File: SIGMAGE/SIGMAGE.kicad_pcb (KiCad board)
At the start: 6 copper layers, 100 x 85 mm, 128 parts, among them J1 UJ31CHG2SMTTR, J10 TSW10607GS, J11 HTSW10807GD, J12 HTSW10807GD, J13 HTSW10807GD, J14 HTSW10807GD, J15 HTSW10807GD, J16 HTSW10807GD, J17 HTSW10807GD, J18 HTSW10107GD, J19 HTSW10107GD, J2 SJ63073E, J20 HTSW10107GD, J3 SJ63073E, J4 SJ63073E, J5 SJ63073E, J6 ARJM11D7502ABEW2, J7 TSW10607GS, J8 TSW10607GS, J9 TSW10607GS, U1 MAX8902BATA/V+T, U2 MAX8902BATA/V+T, U3 MAX8902BATA/V+T, U4 OPA1612AIDRGR, U5 PCM1803ADB, U6 OPA1612AIDRGR, U7 PCM1803ADB, U8 STM32F407VGTx, U9 LAN8720ACP, X1 STDCSU18M, X2 STDCSK425M

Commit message: Makin it waaay cheaper and JLCPCB conform
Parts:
- removed C58: 1u, Capacitor_SMD:C_0603_1608Metric
- removed C7, C9: 10u, Capacitor_SMD:C_0603_1608Metric
- removed C8: 10n, Capacitor_SMD:C_0603_1608Metric
- removed FB3: 500 @ 100 MHz, Capacitor_SMD:C_0603_1608Metric
- removed J20: HTSW10107GD, SIGMAGE:HTSW10107GD
- removed R7, R8: 120k, Resistor_SMD:R_0603_1608Metric
- removed U3: MAX8902BATA/V+T, SIGMAGE:MAX8902BATAVT
- C28, C29, C30, C31, C32, C33, C34, C35, C40, C53: moved to B.Cu
- moved J11 324.9 mm to (375.4, 28.8)
- moved J12 324.9 mm to (375.4, 36.4)
- moved J13 324.9 mm to (375.4, 44.1)
- moved C14 139.7 mm to (180.2, 100.8)
- moved C15 138.6 mm to (166.5, 99.5)
- moved C34 106.6 mm to (144.2, 131.0), turned to 180 degrees
- moved C35 104.5 mm to (144.2, 129.5), turned to 180 degrees
- moved C49 102.0 mm to (111.2, 121.8), turned to -90 degrees
- moved C50 98.8 mm to (112.8, 121.8), turned to -90 degrees
- moved J19 98.7 mm to (180.5, 142.5)
- moved D2 98.3 mm to (176.0, 145.5), turned to 90 degrees
- moved C51 98.1 mm to (106.5, 117.5), turned to 90 degrees
- moved C52 98.1 mm to (106.5, 120.5), turned to -90 degrees
- moved D4 97.6 mm to (194.0, 137.2), turned to -90 degrees
- moved R5 96.5 mm to (173.0, 146.0), turned to 180 degrees
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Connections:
- J11 pad 1: GPIO_PE14 -> unconnected-(J11-Pad1)
- J11 pad 10: GPIO_PE7 -> unconnected-(J11-Pad10)
- J11 pad 11: GPIO_PB2 -> unconnected-(J11-Pad11)
- J11 pad 12: GPIO_PB1 -> unconnected-(J11-Pad12)
- J11 pad 13: GPIO_PB0 -> unconnected-(J11-Pad13)
- J11 pad 14: GPIO_PA6 -> unconnected-(J11-Pad14)
- J11 pad 15: GPIO_PA5 -> unconnected-(J11-Pad15)
- J11 pad 16: GPIO_PA3 -> unconnected-(J11-Pad16)
- J11 pad 2: GPIO_PE12 -> unconnected-(J11-Pad2)
- J11 pad 3: GPIO_PE15 -> unconnected-(J11-Pad3)
- J11 pad 4: GPIO_PE13 -> unconnected-(J11-Pad4)
- J11 pad 5: GPIO_PB14 -> unconnected-(J11-Pad5)
- J11 pad 6: GPIO_PE11 -> unconnected-(J11-Pad6)
- J11 pad 7: GPIO_PE10 -> unconnected-(J11-Pad7)
- J11 pad 8: GPIO_PE9 -> unconnected-(J11-Pad8)
- J11 pad 9: GPIO_PE8 -> unconnected-(J11-Pad9)
- J12 pad 1: GPIO_PC3 -> unconnected-(J12-Pad1)
- J12 pad 10: GPIO_PD5 -> unconnected-(J12-Pad10)
- J12 pad 11: GPIO_PE0 -> unconnected-(J12-Pad11)
- J12 pad 12: GPIO_PD7 -> unconnected-(J12-Pad12)
- J12 pad 13: GPIO_PE4 -> unconnected-(J12-Pad13)
- J12 pad 14: GPIO_PE1 -> unconnected-(J12-Pad14)
- J12 pad 15: GPIO_PE2 -> unconnected-(J12-Pad15)
- J12 pad 16: GPIO_PE3 -> unconnected-(J12-Pad16)
- J12 pad 2: GPIO_PA0 -> unconnected-(J12-Pad2)
- J12 pad 3: GPIO_PC0 -> unconnected-(J12-Pad3)
- J12 pad 4: GPIO_PC2 -> unconnected-(J12-Pad4)
- J12 pad 5: GPIO_PC14 -> unconnected-(J12-Pad5)
- J12 pad 6: GPIO_PC15 -> unconnected-(J12-Pad6)
- J12 pad 7: GPIO_PE5 -> unconnected-(J12-Pad7)
- J12 pad 8: GPIO_PE6 -> unconnected-(J12-Pad8)
- J12 pad 9: GPIO_PD6 -> unconnected-(J12-Pad9)
- J13 pad 1: GPIO_PC11 -> unconnected-(J13-Pad1)
- J13 pad 10: GPIO_PD10 -> unconnected-(J13-Pad10)
- J13 pad 11: GPIO_PD4 -> unconnected-(J13-Pad11)
- J13 pad 12: GPIO_PD8 -> unconnected-(J13-Pad12)
- J13 pad 13: GPIO_PD0 -> unconnected-(J13-Pad13)
- J13 pad 14: GPIO_PD3 -> unconnected-(J13-Pad14)
- J13 pad 15: GPIO_PD1 -> unconnected-(J13-Pad15)
- J13 pad 16: GPIO_PD2 -> unconnected-(J13-Pad16)
- J13 pad 2: GPIO_PC8 -> unconnected-(J13-Pad2)
- J13 pad 3: GPIO_PC9 -> unconnected-(J13-Pad3)
- J13 pad 4: GPIO_PD15 -> unconnected-(J13-Pad4)
- J13 pad 5: GPIO_PD13 -> unconnected-(J13-Pad5)
- J13 pad 6: GPIO_PD14 -> unconnected-(J13-Pad6)
- J13 pad 7: GPIO_PD11 -> unconnected-(J13-Pad7)
- J13 pad 8: GPIO_PD12 -> unconnected-(J13-Pad8)
- J13 pad 9: GPIO_PD9 -> unconnected-(J13-Pad9)
- J14 pad 1: +3V3 -> +5V
- J14 pad 10: +3V3 -> +5V
- J14 pad 11: +3V3 -> +5V
- J14 pad 12: +3V3 -> +5V
- J14 pad 13: +3V3 -> +5V
- J14 pad 14: +3V3 -> +5V
- J14 pad 15: +3V3 -> +5V
- J14 pad 16: +3V3 -> +5V
- J14 pad 2: +3V3 -> +5V
- J14 pad 3: +3V3 -> +5V
- J14 pad 4: +3V3 -> +5V
- J14 pad 5: +3V3 -> +5V
- J14 pad 6: +3V3 -> +5V
- J14 pad 7: +3V3 -> +5V
- J14 pad 8: +3V3 -> +5V
- J14 pad 9: +3V3 -> +5V
- J15 pad 1: +2V5 -> +3V3
- J15 pad 10: +2V5 -> +3V3
- J15 pad 11: +2V5 -> +3V3
- J15 pad 12: +2V5 -> +3V3
- J15 pad 13: +2V5 -> +3V3
- J15 pad 14: +2V5 -> +3V3
- J15 pad 15: +2V5 -> +3V3
- J15 pad 16: +2V5 -> +3V3
- J15 pad 2: +2V5 -> +3V3
- J15 pad 3: +2V5 -> +3V3
- J15 pad 4: +2V5 -> +3V3
- J15 pad 5: +2V5 -> +3V3
- J15 pad 6: +2V5 -> +3V3
- J15 pad 7: +2V5 -> +3V3
- J15 pad 8: +2V5 -> +3V3
- J15 pad 9: +2V5 -> +3V3
- J16 pad 1: +1V2 -> +2V5
- J16 pad 10: +1V2 -> +2V5
- J16 pad 11: +1V2 -> +2V5
- J16 pad 12: +1V2 -> +2V5
- J16 pad 13: +1V2 -> +2V5
- J16 pad 14: +1V2 -> +2V5
- J16 pad 15: +1V2 -> +2V5
- J16 pad 16: +1V2 -> +2V5
- J16 pad 2: +1V2 -> +2V5
- J16 pad 3: +1V2 -> +2V5
- J16 pad 4: +1V2 -> +2V5
- J16 pad 5: +1V2 -> +2V5
- J16 pad 6: +1V2 -> +2V5
- J16 pad 7: +1V2 -> +2V5
- J16 pad 8: +1V2 -> +2V5
- J16 pad 9: +1V2 -> +2V5
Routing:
- net GND: track 157.6 -> 0.00 mm, vias 47 -> 0
- net +5V: track 122.0 -> 0.00 mm, vias 12 -> 0
- net GPIO_PD0: track 78.9 -> 0.00 mm, vias 1 -> 0
- net GPIO_PD4: track 73.5 -> 0.00 mm, vias 1 -> 0
- net GPIO_PD1: track 72.1 -> 0.00 mm, vias 1 -> 0
- net GPIO_PD3: track 70.3 -> 0.00 mm, vias 1 -> 0
- net GPIO_PD2: track 67.8 -> 0.00 mm, vias 1 -> 0
- net +3V3: track 70.1 -> 10.6 mm, vias 17 -> 0
- net GPIO_PC11: track 56.6 -> 0.00 mm, vias 1 -> 0
- net GPIO_PD6: track 52.4 -> 0.00 mm, vias 1 -> 0
- net GPIO_PD13: track 51.8 -> 0.00 mm, vias 1 -> 0
- net GPIO_PD11: track 51.8 -> 0.00 mm, vias 1 -> 0
- net GPIO_PE0: track 51.6 -> 0.00 mm, vias 1 -> 0
- net PHY_TXD0: track 51.3 -> 0.00 mm, vias 2 -> 0
- net GPIO_PD9: track 51.1 -> 0.00 mm, vias 1 -> 0
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- added copper zone on F.Cu, net +5V
- added copper zone on F.Cu, net Net-(C56-Pad1)
- added copper zone on F.Cu, net Net-(C57-Pad1)
- added copper zone on F.Cu, net Net-(D1-A)
- added copper zone on F.Cu, net Net-(D2-A)
- added copper zone on F.Cu, net Net-(D4-A)
- added copper zone on F.Cu, net Net-(R2-Pad2)
- added copper zone on F.Cu, net Net-(R32-Pad1)
- added copper zone on F.Cu, net Net-(U1-BYP)
- added copper zone on F.Cu, net Net-(U1-FB)
- added copper zone on F.Cu, net Net-(U1-OUT)
- added copper zone on F.Cu, net Net-(U2-BYP)
- added copper zone on F.Cu, net Net-(U2-FB)
- added copper zone on F.Cu, net Net-(U2-OUT)
- added copper zone on F.Cu, net Net-(U9-VDDCR)
- added copper zone on F.Cu, net VBUS
- added copper zone on F.Cu, net VREF+
- removed copper zone on In3.Cu, net +1V2
- removed copper zone on In3.Cu, net +2V5
- removed copper zone on In3.Cu, net +3V3
- removed copper zone on In3.Cu, net +5V
- removed copper zone on In2.Cu, net GND
- removed copper zone on In3.Cu, net VBUS
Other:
- board size 100 x 85 mm -> 100 x 90 mm
- copper layers 6 -> 2

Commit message: Some routing..
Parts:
- removed J11, J12, J13: HTSW10807GD, SIGMAGE:HTSW10807GD
- moved R31 1.75 mm to (117.0, 114.8), turned to 180 degrees
- moved C47 1.25 mm to (117.0, 113.2)
- moved C43 0.50 mm to (146.0, 136.8)
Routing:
- net PHY_TXEN: track 0.00 -> 44.6 mm, vias 0 -> 2
- net PHY_NRST: track 3.03 -> 43.0 mm, vias 0 -> 2
- net PHY_CRS_DV: track 0.00 -> 35.9 mm, vias 0 -> 2
- net PHY_TXD0: track 0.00 -> 31.8 mm, vias 0 -> 2
- net PHY_REFCLK: track 0.00 -> 29.0 mm, vias 0 -> 2
- net PHY_MDIO: track 0.00 -> 28.7 mm, vias 0 -> 2
- net PHY_MDC: track 0.00 -> 22.2 mm, vias 0 -> 2
- net PHY_TXD1: track 0.00 -> 21.3 mm
- net Net-(U8-VCAP_2): track 2.77 -> 0.00 mm
- net Net-(U8-VCAP_1): track 2.30 -> 0.00 mm
- added copper zone on F.Cu, net +3V3
- added copper zone on F.Cu, net Net-(U8-VCAP_1)
- added copper zone on F.Cu, net Net-(U8-VCAP_2)

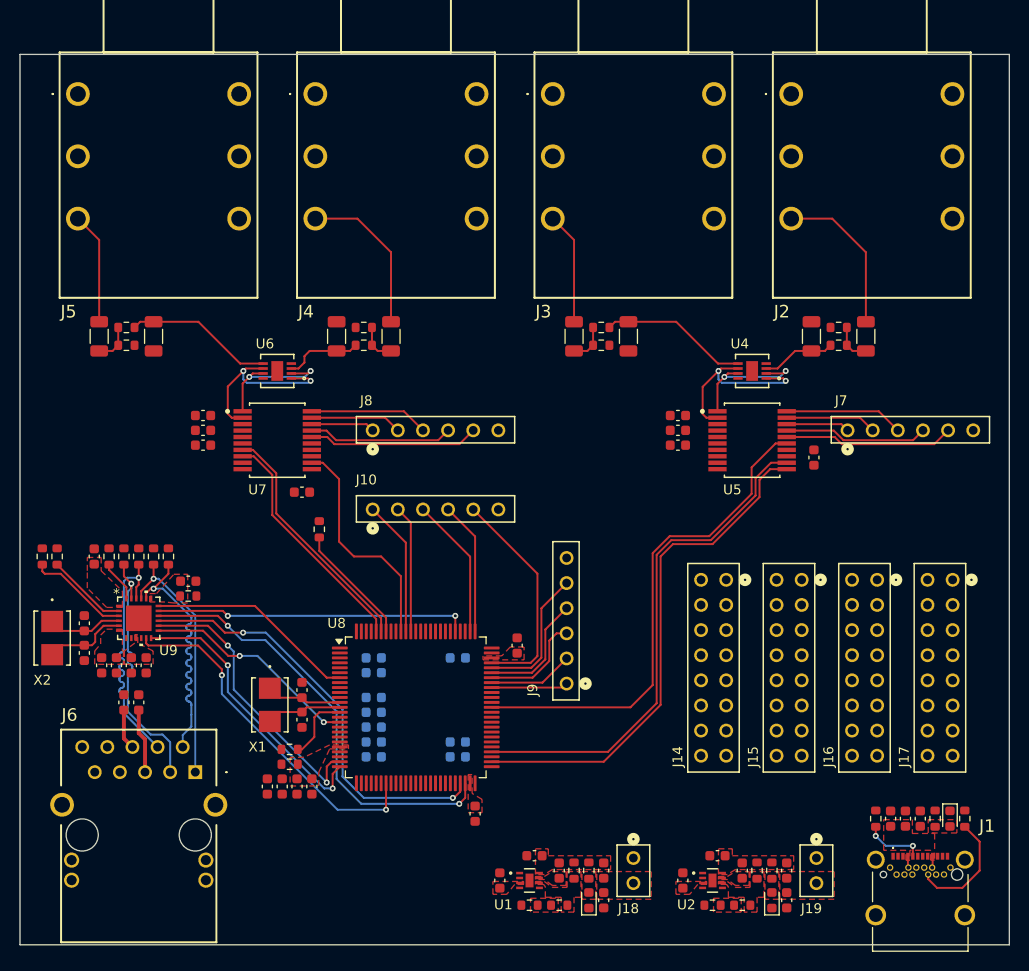
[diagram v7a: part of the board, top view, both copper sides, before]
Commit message: Added GND planes and started power dist
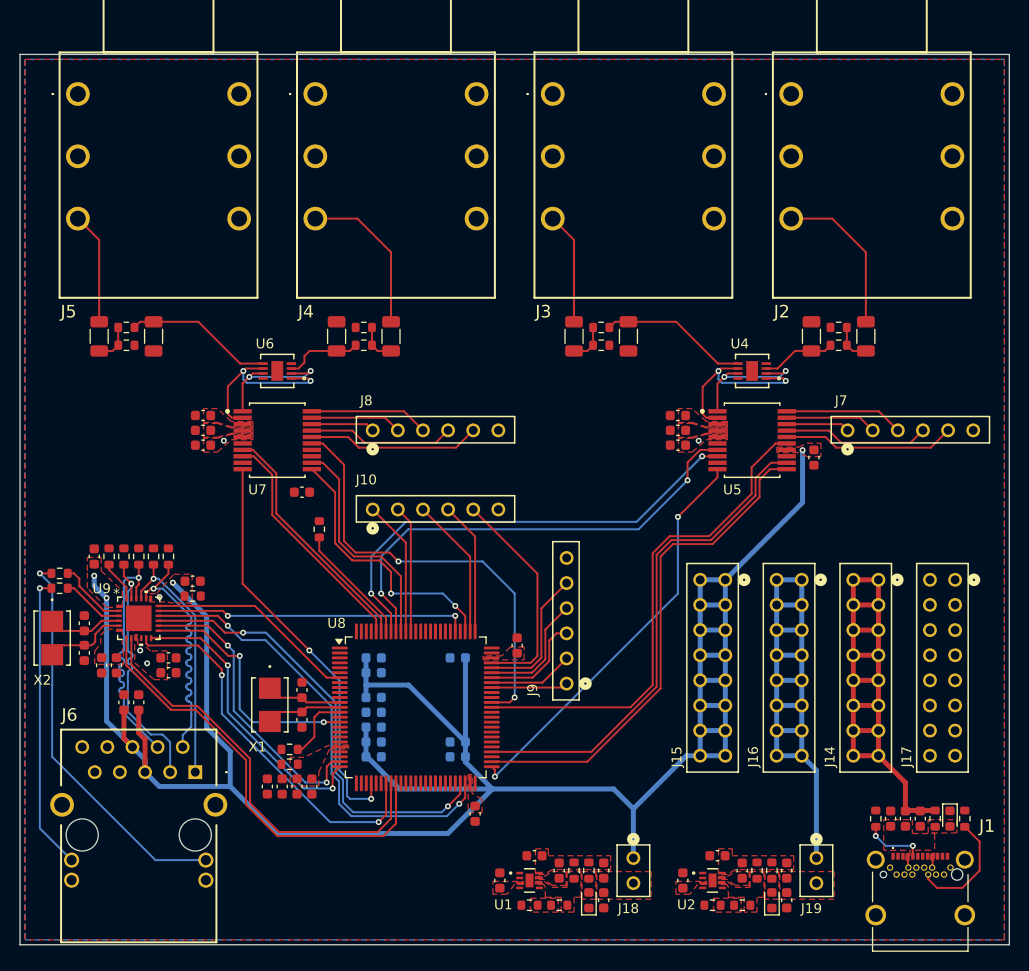
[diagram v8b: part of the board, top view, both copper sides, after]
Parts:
- moved J14 15.4 mm to (185.5, 122.0)
- moved J15 7.72 mm to (170.0, 122.0)
- moved J16 7.62 mm to (177.8, 122.0)
- moved C49 3.82 mm to (115.0, 122.5), turned to 0 degrees
- moved R24 3.66 mm to (104.0, 114.0), turned to 0 degrees
- moved C50 2.37 mm to (115.0, 121.0), turned to 0 degrees
- moved R25 1.73 mm to (104.0, 112.5), turned to 0 degrees
- moved C47 0.45 mm to (117.5, 113.2)
- moved R31 0.45 mm to (117.5, 114.8)
- moved J17 0.25 mm to (193.2, 122.0)
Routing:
- net +3V3: track 10.6 -> 244.3 mm, vias 0 -> 7
- net +2V5: track 0.00 -> 66.8 mm
- net +5V: track 0.00 -> 65.6 mm, vias 0 -> 2
- net ADC1_PDWN: track 0.00 -> 47.7 mm, vias 0 -> 2
- net ADC1_BYPAS: track 0.00 -> 47.6 mm, vias 0 -> 2
- net PHY_RXD1: track 0.00 -> 44.4 mm
- net ADC2_SCKI: track 0.00 -> 44.3 mm, vias 0 -> 2
- net PHY_RXD0: track 0.00 -> 42.7 mm
- net ADC2_LRCK: track 0.00 -> 41.5 mm, vias 0 -> 2
- net ADC1_LRCK: track 0.00 -> 41.5 mm, vias 0 -> 2
- net Net-(J6-A_YELLOW): track 0.00 -> 40.1 mm, vias 0 -> 1
- net Net-(J6-A_GREEN): track 0.00 -> 30.0 mm, vias 0 -> 1
- net ADC2_BCK: track 0.00 -> 27.5 mm, vias 0 -> 2
- net Net-(U9-LED1/*REGOFF): track 10.3 -> 6.33 mm
- net PHY_MDC: track 22.2 -> 25.3 mm
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- added copper zone on B.Cu, net GND
- added copper zone on F.Cu, net GND
- added copper zone on F.Cu, net Net-(U5-VREF1)
- added copper zone on F.Cu, net Net-(U5-VREF2)
- added copper zone on F.Cu, net Net-(U7-VREF1)
- added copper zone on F.Cu, net Net-(U7-VREF2)
